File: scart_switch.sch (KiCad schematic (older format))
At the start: 48 parts, among them J0 BARREL_JACK, U0 CBT3245, U1 CBT3245, U10 7805, U2 CBT3245, U3 CBT3245, U4 CBT3245, U5 CBT3245, U6 CBT3245, U7 CBT3245, U9 TSOP382xx

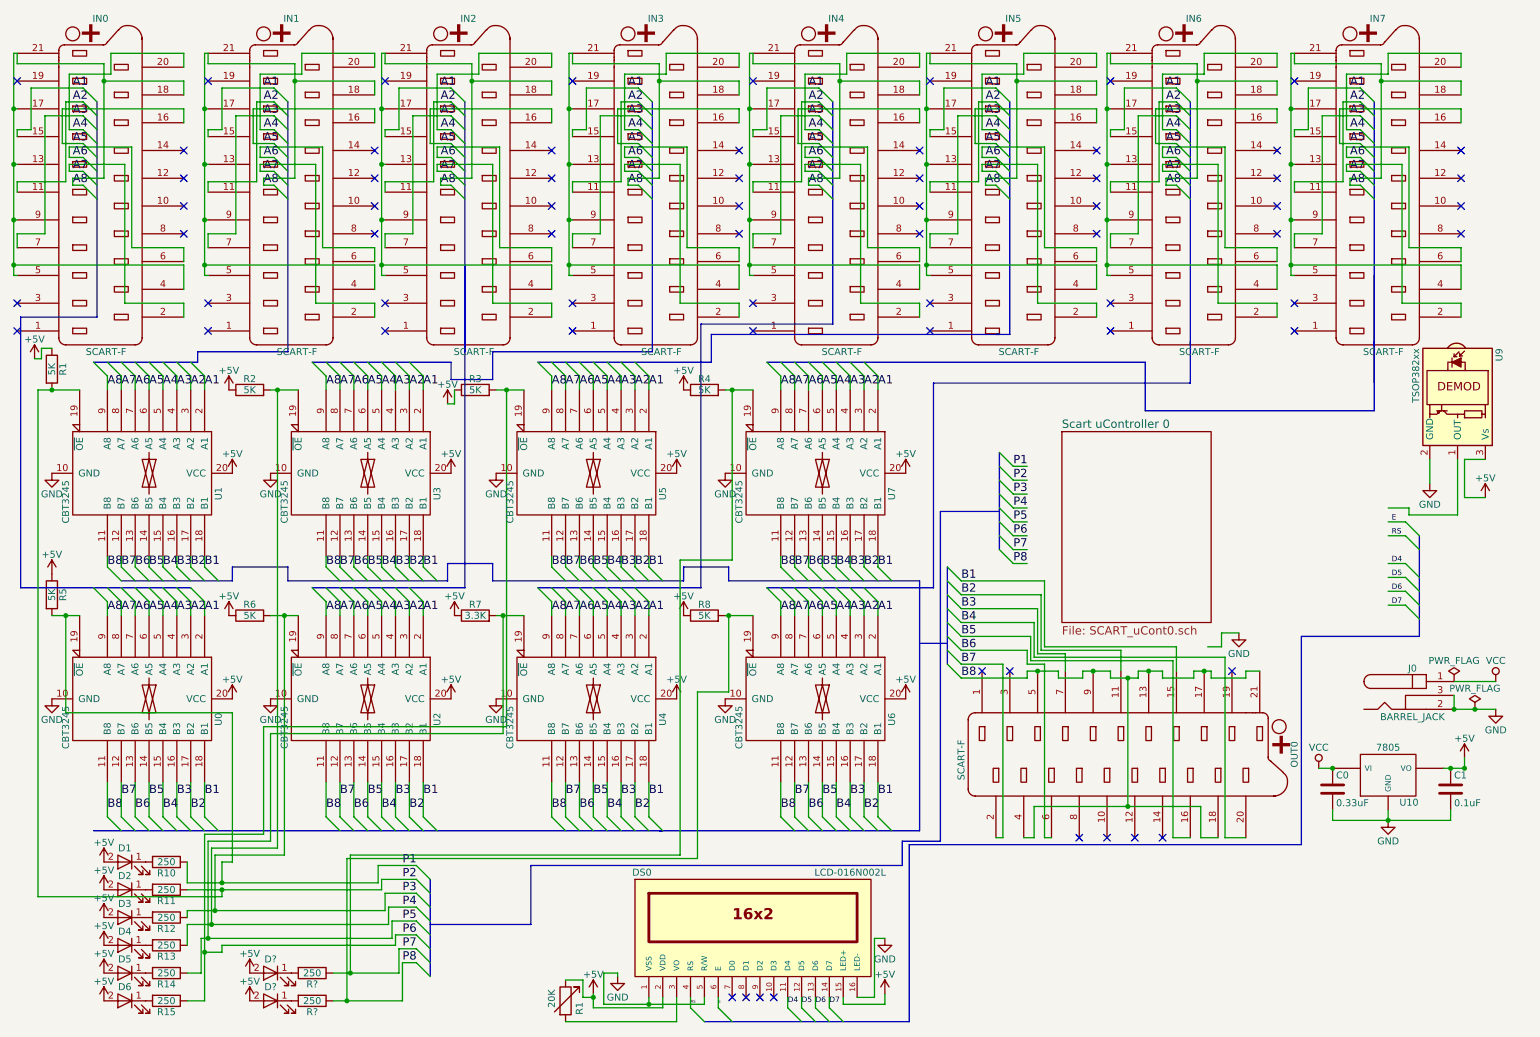
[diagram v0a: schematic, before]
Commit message: initial commit for no ir branch
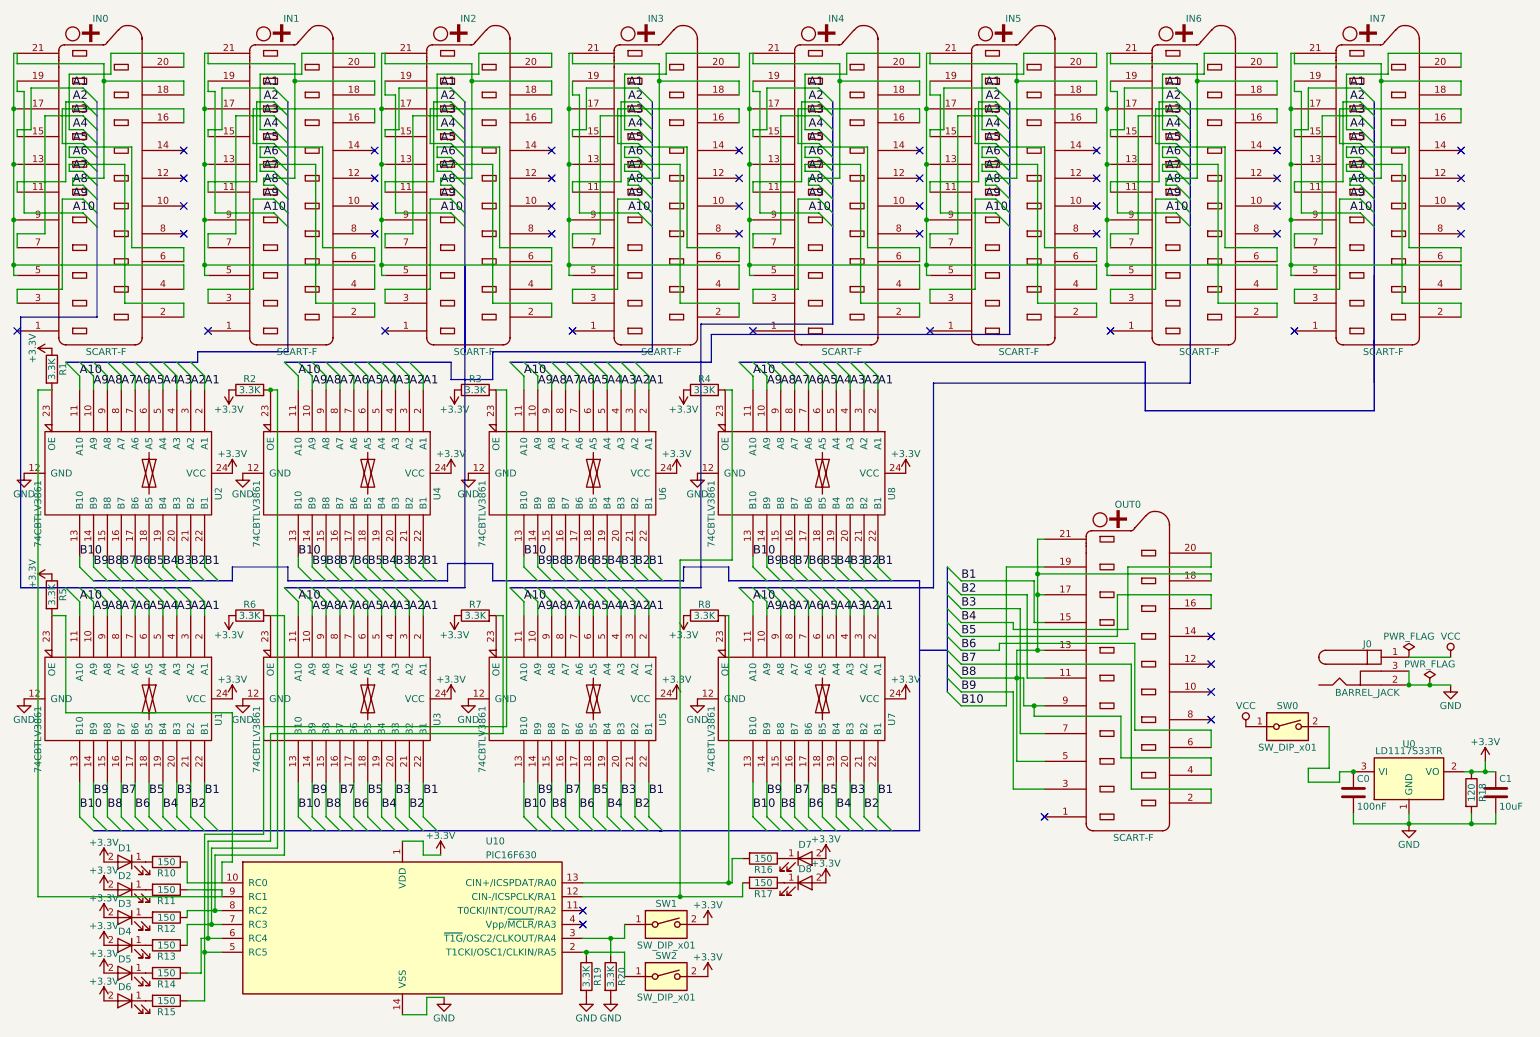
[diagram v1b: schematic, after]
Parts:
- removed D? (x2): LED, symbol LED
- removed DS0: LCD-016N002L, WC1602A, symbol LCD-016N002L-RESCUE-scart_switch
- removed R1: 20K, symbol R_Variable
- removed R? (x2): 250, symbol R
- removed U0, U1, U2, U3, U4, U5, U6, U7: CBT3245, symbol CBT3245
- removed U10: 7805, symbol 7805
- removed U9: TSOP382xx, Opto-Devices:IRReceiver_Vishay_MINICAST-3pin, symbol TSOP382xx
- added D7, D8: LED, symbol LED
- added R16, R17: 150, symbol R
- added R18: 120, symbol R
- added R19, R20: 3.3K, symbol R
- added SW0, SW1, SW2: SW_DIP_x01, symbol SW_DIP_x01
- added U0: LD1117S33TR, TO_SOT_Packages_SMD:SOT-223, symbol LD1117S33TR
- added U1, U2, U3, U4, U5, U6, U7, U8: 74CBTLV3861, symbol 74CBTLV3861
- added U10: PIC16F630, symbol PIC16F630
- C0: value 0.33uF -> 100nF
- C1: value 0.1uF -> 10uF
- R1, R2, R3, R4, R5, R6, R8: value 5K -> 3.3K
- R10, R11, R12, R13, R14, R15: value 250 -> 150
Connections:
- net A1: now also U1.2 (A1), U2.2 (A1), U3.2 (A1), U4.2 (A1), U5.2 (A1), U6.2 (A1), U7.2 (A1), U8.2 (A1)
- net A2: now also U1.3 (A2), U2.3 (A2), U3.3 (A2), U4.3 (A2), U5.3 (A2), U6.3 (A2), U7.3 (A2), U8.3 (A2)
- net A3: now also U1.4 (A3), U2.4 (A3), U3.4 (A3), U4.4 (A3), U5.4 (A3), U6.4 (A3), U7.4 (A3), U8.4 (A3)
- net A4: now also U1.5 (A4), U2.5 (A4), U3.5 (A4), U4.5 (A4), U5.5 (A4), U6.5 (A4), U7.5 (A4), U8.5 (A4)
- net A5: now also U1.6 (A5), U2.6 (A5), U3.6 (A5), U4.6 (A5), U5.6 (A5), U6.6 (A5), U7.6 (A5), U8.6 (A5)
- net A6: now also U1.7 (A6), U2.7 (A6), U3.7 (A6), U4.7 (A6), U5.7 (A6), U6.7 (A6), U7.7 (A6), U8.7 (A6)
- net A7: now also U1.8 (A7), U2.8 (A7), U3.8 (A7), U4.8 (A7), U5.8 (A7), U6.8 (A7), U7.8 (A7), U8.8 (A7)
- net A8: now also U1.9 (A8), U2.9 (A8), U3.9 (A8), U4.9 (A8), U5.9 (A8), U6.9 (A8), U7.9 (A8), U8.9 (A8)
- net B1: now also U1.22 (B1), U2.22 (B1), U3.22 (B1), U4.22 (B1), U5.22 (B1), U6.22 (B1), U7.22 (B1), U8.22 (B1)
- net B2: now also U1.21 (B2), U2.21 (B2), U3.21 (B2), U4.21 (B2), U5.21 (B2), U6.21 (B2), U7.21 (B2), U8.21 (B2)
- net B3: now also U1.20 (B3), U2.20 (B3), U3.20 (B3), U4.20 (B3), U5.20 (B3), U6.20 (B3), U7.20 (B3), U8.20 (B3)
- net B4: now also U1.19 (B4), U2.19 (B4), U3.19 (B4), U4.19 (B4), U5.19 (B4), U6.19 (B4), U7.19 (B4), U8.19 (B4)
- net B5: now also U1.18 (B5), U2.18 (B5), U3.18 (B5), U4.18 (B5), U5.18 (B5), U6.18 (B5), U7.18 (B5), U8.18 (B5)
- net B6: now also U1.17 (B6), U2.17 (B6), U3.17 (B6), U4.17 (B6), U5.17 (B6), U6.17 (B6), U7.17 (B6), U8.17 (B6)
- net B7: now also U1.16 (B7), U2.16 (B7), U3.16 (B7), U4.16 (B7), U5.16 (B7), U6.16 (B7), U7.16 (B7), U8.16 (B7)
- net B8: now also U1.15 (B8), U2.15 (B8), U3.15 (B8), U4.15 (B8), U5.15 (B8), U6.15 (B8), U7.15 (B8), U8.15 (B8)
- net GND: now also R18.2, R19.2, R20.2, U0.1 (GND), U1.12 (GND), U10.14 (VSS), U2.12 (GND), U3.12 (GND), U4.12 (GND), U5.12 (GND), U6.12 (GND), U7.12 (GND), U8.12 (GND)
- net VCC: now also SW0.1; no longer C0.1
- net A10: now reaches IN0.19 (P19)
- net A10: now also IN1.19 (P19), IN2.19 (P19), IN3.19 (P19), IN4.19 (P19), IN5.19 (P19), IN6.19 (P19), IN7.19 (P19), U1.11 (A10), U2.11 (A10), U3.11 (A10), U4.11 (A10), U5.11 (A10), U6.11 (A10), U7.11 (A10), U8.11 (A10)
- net A9: now reaches IN0.3 (P3)
- net A9: now also IN1.3 (P3), IN2.3 (P3), IN3.3 (P3), IN4.3 (P3), IN5.3 (P3), IN6.3 (P3), IN7.3 (P3), U1.10 (A9), U2.10 (A9), U3.10 (A9), U4.10 (A9), U5.10 (A9), U6.10 (A9), U7.10 (A9), U8.10 (A9)
- net B10: now reaches OUT0.19 (P19)
- net B10: now also U1.13 (B10), U2.13 (B10), U3.13 (B10), U4.13 (B10), U5.13 (B10), U6.13 (B10), U7.13 (B10), U8.13 (B10)
- net B9: now reaches OUT0.3 (P3)
- net B9: now also U1.14 (B9), U2.14 (B9), U3.14 (B9), U4.14 (B9), U5.14 (B9), U6.14 (B9), U7.14 (B9), U8.14 (B9)
- net +5V renamed +3V3
- net +3V3: now also D7.2 (A), D8.2 (A), R18.1, SW1.2, SW2.2, U0.2 (VO), U1.24 (VCC), U10.1 (VDD), U2.24 (VCC), U3.24 (VCC), U4.24 (VCC), U5.24 (VCC), U6.24 (VCC), U7.24 (VCC), U8.24 (VCC)
- net P1: no longer names the net of R10.1, R5.2
- net P1: now also U1.23 (OE), U10.10 (RC0)
- net P2: no longer names the net of R1.2, R11.1
- net P2: now also U10.9 (RC1), U2.23 (OE)
- net P3: no longer names the net of R12.1, R6.2
- net P3: now also U10.8 (RC2), U3.23 (OE)
- net P4: no longer names the net of R13.1, R2.2
- net P4: now also U10.7 (RC3), U4.23 (OE)
- net P5: no longer names the net of R14.1, R7.2
- net P5: now also U10.6 (RC4), U5.23 (OE)
- net P6: no longer names the net of R15.1, R3.2
- net P6: now also U10.5 (RC5), U6.23 (OE)
- net P7: no longer names the net of R4.2
- net P7: now also R17.2, U10.12 (CIN-/ICSPCLK/RA1), U8.23 (OE)
- net P8: no longer names the net of R8.2
- net P8: now also R16.2, U10.13 (CIN+/ICSPDAT/RA0), U7.23 (OE)
- new net: C0.1, SW0.2, U0.3 (VI)
- new net: R19.1, SW2.1, U10.2 (T1CKI/OSC1/CLKIN/RA5)
- new net: R20.1, SW1.1, U10.3 (~T1G~/OSC2/CLKOUT/RA4)
- new net: D7.1 (K), R16.1
- new net: D8.1 (K), R17.1
- no-connect marks 67 -> 47
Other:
- moved on the sheet: C0, C1, J0, OUT0
